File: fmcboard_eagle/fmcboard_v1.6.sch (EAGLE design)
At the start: 296 parts, among them IC1 OPA699ID, IC10 LM358, IC11 7805DT, IC12 SN74AUC2G66DCTR, IC13 SN74AUC2G66DCTR, IC14 SN74AUC2G66DCTR, IC15 SN74AUC2G66DCTR, IC16 DAC7578SPWR, IC17 SN74AUC2G66DCTR, IC18 SN74AUC2G66DCTR, IC19 SN74AUC2G66DCTR, IC2 DAC7578SPWR, IC20 SN74AUC2G66DCTR, IC21 74AUP2GU04GW, IC22 74AUP2GU04GW, IC23 74AUP2GU04GW, IC24 74AUP2GU04GW, IC25 MC7905ACD2TR4G, IC26 AMS1117-1.8, IC27 LM358, IC28 SN74AUC2G66DCTR, IC29 LM337KVURG3, IC3 LTC6229IMS8E#TRPBF, IC30 SN74AUC2G66DCTR, IC31 SN74AUC2G66DCTR, IC32 SN74AUC2G66DCTR, IC33 LTC6229IMS8E#TRPBF, IC34 74AUP2GU04GW, IC35 74AUP2GU04GW, IC36 TPS5430DDAR, IC37 TPS5430DDAR, IC4 OPA695IDR, IC5 LTC6229IMS8E#TRPBF, IC6 OPA695IDR, IC7 OPA699ID, IC8 LM358, IC9 LM358, J1 8pin, J12 4p-2.54, J13 4p-2.54, J2 ASP-134604-01, J3 2p-2.54, J5 4p-2.54, J8 4p-2.54, J9 2p-2.54

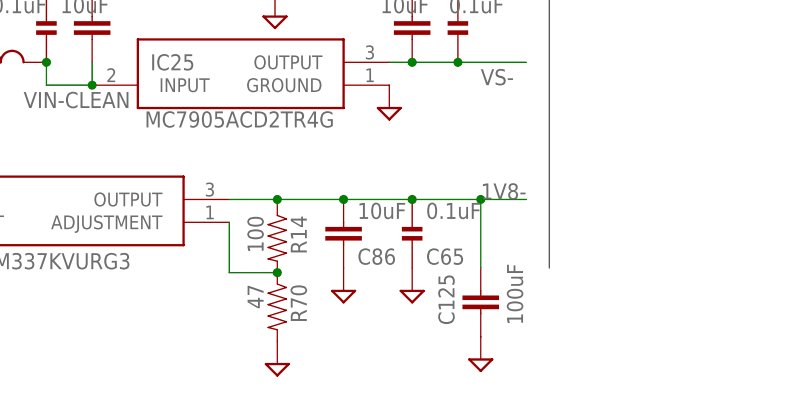
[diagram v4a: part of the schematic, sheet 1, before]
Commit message: Tant only on 1.8- regulator
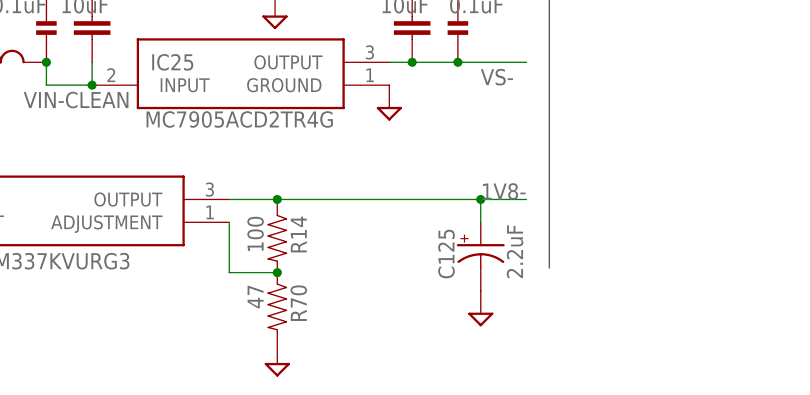
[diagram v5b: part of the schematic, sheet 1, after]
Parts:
- removed C65: 0.1uF, passives:CAPACITOR0402_CAP
- removed C86: 10uF, rcl:C-EUC0805
- C125: value 100uF -> 2.2uF; device rcl:C-EUC1206K -> SparkFun-Capacitors:CAP_POL1206
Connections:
- net 1V8-: now also C125.+; no longer C125.1, C65.1, C86.1
- net GND: now also C125.-; no longer C125.2, C65.2, C86.2
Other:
- note added: "Tant only! Case 3216"
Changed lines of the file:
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@@
 <part name="C33" library="passives" deviceset="CAPACITOR" device="0402_CAP" value="0.1uF"/>
 <part name="SUPPLY76" library="supply2" library_urn="urn:adsk.eagle:library:372" deviceset="GND" device=""/>
-<part name="C65" library="passives" deviceset="CAPACITOR" device="0402_CAP" value="0.1uF"/>
-<part name="SUPPLY83" library="supply2" library_urn="urn:adsk.eagle:library:372" deviceset="GND" device=""/>
 <part name="R79" library="passives" deviceset="RESISTOR" device="0402_RES" value="1k"/>
 <part name="R85" library="passives" deviceset="RESISTOR" device="0402_RES" value="1k"/>
@@
 <part name="C77" library="rcl" library_urn="urn:adsk.eagle:library:334" deviceset="C-EU" device="C0805" package3d_urn="urn:adsk.eagle:package:23617/2" value="10uF"/>
 <part name="SUPPLY25" library="supply2" library_urn="urn:adsk.eagle:library:372" deviceset="GND" device=""/>
-<part name="C86" library="rcl" library_urn="urn:adsk.eagle:library:334" deviceset="C-EU" device="C0805" package3d_urn="urn:adsk.eagle:package:23617/2" value="10uF"/>
-<part name="SUPPLY45" library="supply2" library_urn="urn:adsk.eagle:library:372" deviceset="GND" device=""/>
 <part name="R14" library="passives" deviceset="RESISTOR" device="0402_RES" value="100"/>
 <part name="R70" library="passives" deviceset="RESISTOR" device="0402_RES" value="47"/>
@@
 <part name="R73" library="passives" deviceset="RESISTOR" device="0402_RES" value="10k"/>
 <part name="R84" library="passives" deviceset="RESISTOR" device="0402_RES" value="1k"/>
-<part name="C125" library="rcl" library_urn="urn:adsk.eagle:library:334" deviceset="C-EU" device="C1206K" package3d_urn="urn:adsk.eagle:package:23682/2" value="100uF"/>
+<part name="C125" library="SparkFun-Capacitors" deviceset="CAP_POL" device="1206" value="2.2uF"/>
 <part name="D2" library="SparkFun-DiscreteSemi" library_urn="urn:adsk.eagle:library:514" deviceset="DIODE-SCHOTTKY" device="-B340A" package3d_urn="urn:adsk.eagle:package:38443/1" value="B340A">
 <attribute name="LCSC" value="C64982"/>
@@
 <text x="-2.54" y="-22.86" size="1.778" layer="90">-1.25V x (1+47/100) = -1.84V</text>
 <text x="-71.12" y="50.8" size="1.778" layer="90">1.8V regulator</text>
+<text x="55.88" y="-25.4" size="1.778" layer="90">Tant only!
+Case 3216</text>
 </plain>
 <instances>
@@
 </instance>
 <instance part="SUPPLY76" gate="GND" x="-7.62" y="-20.32" smashed="yes"/>
-<instance part="C65" gate="G$1" x="53.34" y="-10.16" smashed="yes">
-<attribute name="NAME" x="54.864" y="-14.859" size="1.778" layer="95"/>
-<attribute name="VALUE" x="54.864" y="-9.779" size="1.778" layer="96"/>
-</instance>
-<instance part="SUPPLY83" gate="GND" x="53.34" y="-17.78" smashed="yes"/>
 <instance part="C77" gate="G$1" x="-15.24" y="-12.7" smashed="yes">
 <attribute name="NAME" x="-13.716" y="-12.319" size="1.778" layer="95"/>
@@
 </instance>
 <instance part="SUPPLY25" gate="GND" x="-15.24" y="-20.32" smashed="yes"/>
-<instance part="C86" gate="G$1" x="45.72" y="-10.16" smashed="yes">
-<attribute name="NAME" x="47.244" y="-14.859" size="1.778" layer="95"/>
-<attribute name="VALUE" x="47.244" y="-9.779" size="1.778" layer="96"/>
-</instance>
-<instance part="SUPPLY45" gate="GND" x="45.72" y="-17.78" smashed="yes"/>
 <instance part="R14" gate="G$1" x="38.354" y="-13.208" smashed="yes" rot="R270">
 <attribute name="NAME" x="39.8526" y="-9.398" size="1.778" layer="95" rot="R270"/>
@@
 <attribute name="VALUE" x="44.704" y="1.27" size="1.778" layer="96" rot="R180" align="center-left"/>
 </instance>
-<instance part="SUPPLY125" gate="GND" x="60.96" y="-25.4" smashed="yes"/>
+<instance part="SUPPLY125" gate="GND" x="60.96" y="-20.32" smashed="yes"/>
 <instance part="R87" gate="G$1" x="144.78" y="91.44" smashed="yes">
 <attribute name="VALUE" x="140.97" y="88.138" size="1.778" layer="96"/>
@@
 <attribute name="VALUE" x="140.97" y="75.438" size="1.778" layer="96"/>
 </instance>
-<instance part="C125" gate="G$1" x="60.96" y="-17.78" smashed="yes">
-<attribute name="NAME" x="57.15" y="-21.59" size="1.778" layer="95" rot="R90" align="center-left"/>
-<attribute name="VALUE" x="64.77" y="-21.59" size="1.778" layer="96" rot="R90" align="center-left"/>
+<instance part="C125" gate="G$1" x="60.96" y="-12.7" smashed="yes">
+<attribute name="NAME" x="57.15" y="-16.51" size="1.778" layer="95" rot="R90" align="center-left"/>
+<attribute name="VALUE" x="64.77" y="-16.51" size="1.778" layer="96" rot="R90" align="center-left"/>
 </instance>
 <instance part="C110" gate="G$1" x="25.4" y="35.56" smashed="yes">
@@
 </segment>
 <segment>
-<pinref part="C65" gate="G$1" pin="2"/>
-<pinref part="SUPPLY83" gate="GND" pin="GND"/>
-</segment>
-<segment>
 <pinref part="C77" gate="G$1" pin="2"/>
 <pinref part="SUPPLY25" gate="GND" pin="GND"/>
-</segment>
-<segment>
-<pinref part="C86" gate="G$1" pin="2"/>
-<pinref part="SUPPLY45" gate="GND" pin="GND"/>
 </segment>
 <segment>
@@
 </segment>
 <segment>
-<pinref part="C125" gate="G$1" pin="2"/>
+<pinref part="C125" gate="G$1" pin="-"/>
 <pinref part="SUPPLY125" gate="GND" pin="GND"/>
 </segment>
@@
 <segment>
 <pinref part="R14" gate="G$1" pin="1"/>
-<pinref part="C65" gate="G$1" pin="1"/>
-<wire x1="53.34" y1="-7.62" x2="60.96" y2="-7.62" width="0.1524" layer="91"/>
-<junction x="53.34" y="-7.62"/>
 <wire x1="60.96" y1="-7.62" x2="66.04" y2="-7.62" width="0.1524" layer="91"/>
-<wire x1="45.72" y1="-7.62" x2="53.34" y2="-7.62" width="0.1524" layer="91"/>
-<pinref part="C86" gate="G$1" pin="1"/>
-<junction x="45.72" y="-7.62"/>
-<wire x1="45.72" y1="-7.62" x2="38.354" y2="-7.62" width="0.1524" layer="91"/>
+<wire x1="38.354" y1="-7.62" x2="60.96" y2="-7.62" width="0.1524" layer="91"/>
 <wire x1="38.354" y1="-7.62" x2="38.354" y2="-8.128" width="0.1524" layer="91"/>
 <junction x="38.354" y="-7.62"/>
@@
 <wire x1="33.02" y1="-7.62" x2="38.354" y2="-7.62" width="0.1524" layer="91"/>
 <label x="60.96" y="-7.62" size="1.778" layer="95"/>
-<pinref part="C125" gate="G$1" pin="1"/>
-<wire x1="60.96" y1="-15.24" x2="60.96" y2="-7.62" width="0.1524" layer="91"/>
+<pinref part="C125" gate="G$1" pin="+"/>
+<wire x1="60.96" y1="-10.16" x2="60.96" y2="-7.62" width="0.1524" layer="91"/>
 <junction x="60.96" y="-7.62"/>
 </segment>

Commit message: V holes
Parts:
- removed J3, J9: 2p-2.54, Seeed-Connector:DIP-BLACK-MALE-HEADER-VERT(2P-2.54)
- added J4: 4p-2.54, Seeed-Connector:DIP-BLACK-FEMALE-HEADER-VERT(4P-2.54)
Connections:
- net 12V: now also J4.P$1; no longer J9.1
- net 1V8: no longer J12.P$1
- net GND: now also J12.P$1, J4.P$3, J4.P$4; no longer J3.1, J3.2
- net VIN: now also J4.P$2; no longer J9.2

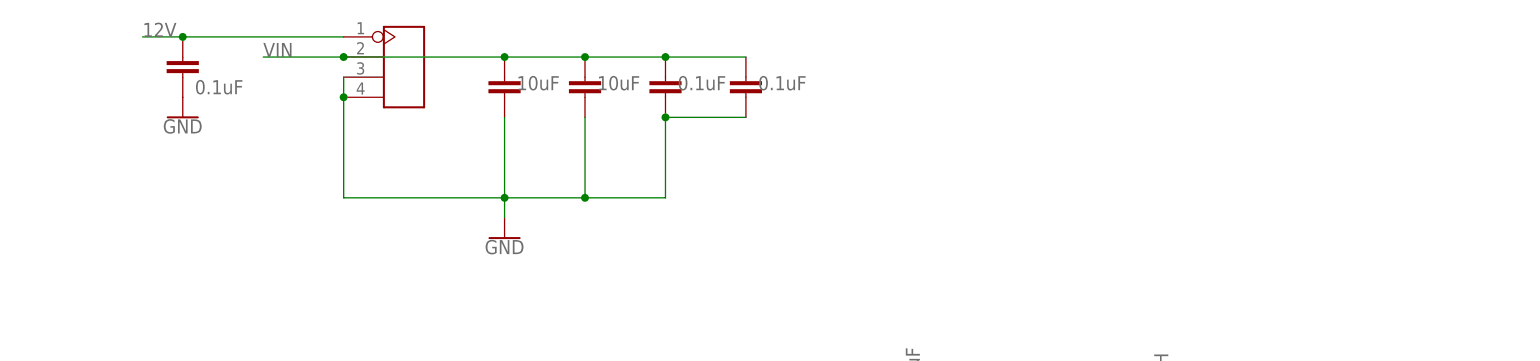
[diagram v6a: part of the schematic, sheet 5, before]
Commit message: smd headers
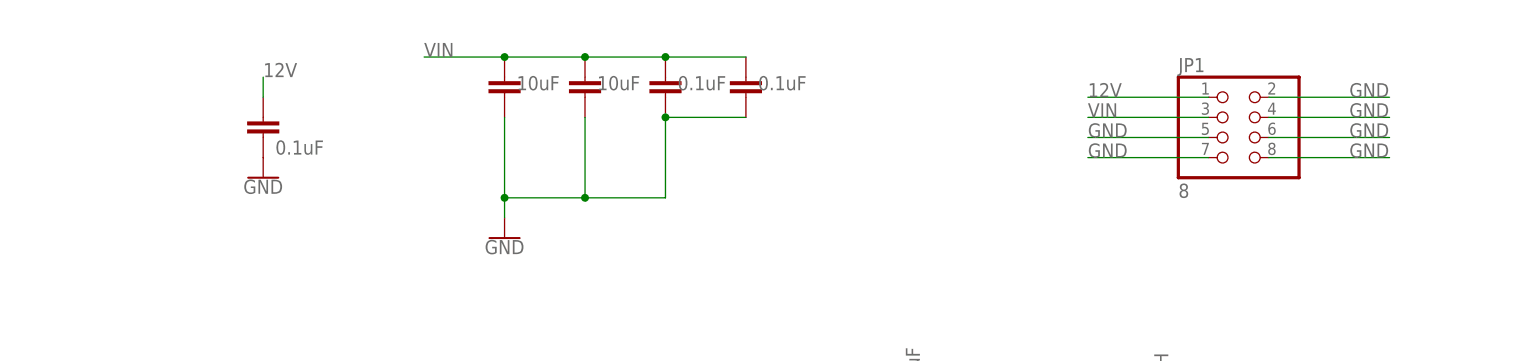
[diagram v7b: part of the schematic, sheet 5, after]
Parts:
- removed J1: 8pin, SparkFun-Connectors:CONN_08"
- removed J4: 4p-2.54, Seeed-Connector:DIP-BLACK-FEMALE-HEADER-VERT(4P-2.54)
- added JP1, JP2: 8, pinhead+:PINHD-2X4SMT
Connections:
- net 12V: now also JP1.1; no longer J4.P$1
- net AR_5V: now also JP2.8; no longer J1.1
- net GND: now also JP1.2, JP1.4, JP1.5, JP1.6, JP1.7, JP1.8, JP2.1, JP2.2, JP2.4, JP2.5; no longer J1.3, J1.4, J1.6, J1.8, J4.P$3, J4.P$4
- net VIN: now also JP1.3; no longer J4.P$2
- net VIN+: now also JP2.7; no longer J1.5
- net VIN-: now also JP2.3; no longer J1.7
- net VS+: now also JP2.6; no longer J1.2

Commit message: Revert "smd headers"
This reverts commit 89ab3707157d78c83d60aa2d6a39565f5008c414.
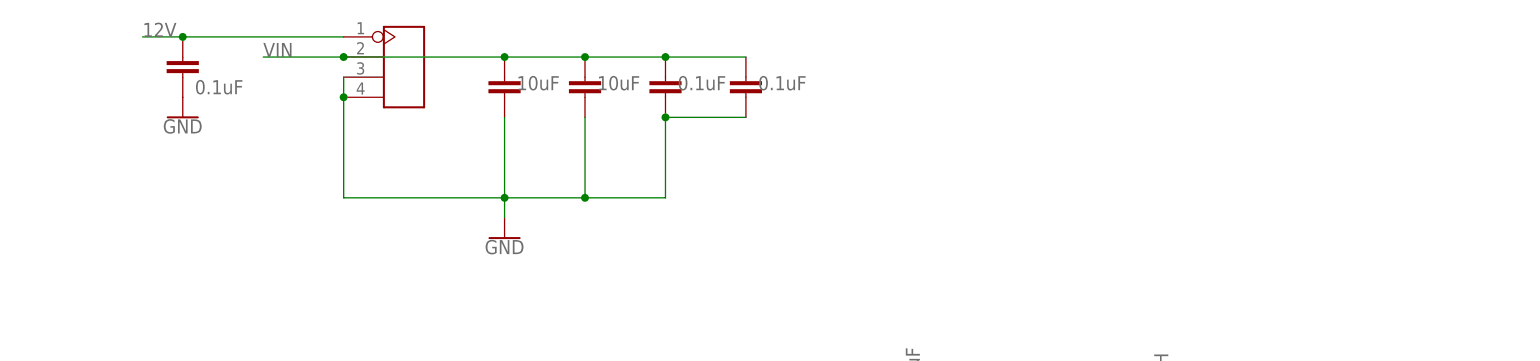
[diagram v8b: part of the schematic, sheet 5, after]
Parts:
- removed JP1, JP2: 8, pinhead+:PINHD-2X4SMT
- added J1: 8pin, SparkFun-Connectors:CONN_08"
- added J4: 4p-2.54, Seeed-Connector:DIP-BLACK-FEMALE-HEADER-VERT(4P-2.54)
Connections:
- net 12V: now also J4.P$1; no longer JP1.1
- net AR_5V: now also J1.1; no longer JP2.8
- net GND: now also J1.3, J1.4, J1.6, J1.8, J4.P$3, J4.P$4; no longer JP1.2, JP1.4, JP1.5, JP1.6, JP1.7, JP1.8, JP2.1, JP2.2, JP2.4, JP2.5
- net VIN: now also J4.P$2; no longer JP1.3
- net VIN+: now also J1.5; no longer JP2.7
- net VIN-: now also J1.7; no longer JP2.3
- net VS+: now also J1.2; no longer JP2.6
